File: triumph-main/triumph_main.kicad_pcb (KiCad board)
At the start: 2 copper layers, 99.1 x 86.4 mm, 83 parts, among them J1 JST_XH_vert_01x04, J10 JST_XH_vert_01x04, J2 JST_PH_vert_01x03, J3 JST_PH_vert_01x03, J4 JST_PH_vert_01x06, J5 Conn_BNC, J6 JST_PH_vert_01x03, J7 JST_PH_vert_01x06, J8 JST_PH_vert_01x03, J9 JST_PH_vert_01x03, Q1 J310, U1 LM211P, U2 NE5532AP, U3 NE5532AP, U4 NE5532AP, U5 NE5532AP

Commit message: Add onboard power LEDs
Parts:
- added D3: BLUE, triumph:LED_1206_HandSoldering, F.Cu at (133.1, 63.5)
- added D4: BLUE, triumph:LED_1206_HandSoldering, F.Cu at (156.0, 63.5)
- added R20: 10K, triumph:0805_R_HandSoldering, B.Cu at (133.1, 63.3)
- added R21: 10K, triumph:0805_R_HandSoldering, B.Cu at (156.0, 63.3)
- renumbered C12 to C10, C13 to C11, C14 to C12, C9 to C13, C10 to C14, C11 to C9, R20 to R22, R21 to R23, R22 to R24, R23 to R25
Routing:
- net +12V: track 269.0 -> 277.3 mm
- net -12V: track 247.1 -> 255.3 mm
- net Net-(D4-Pad2): track 0.00 -> 5.15 mm, vias 0 -> 1
- net Net-(D3-Pad1): track 0.00 -> 4.64 mm, vias 0 -> 1

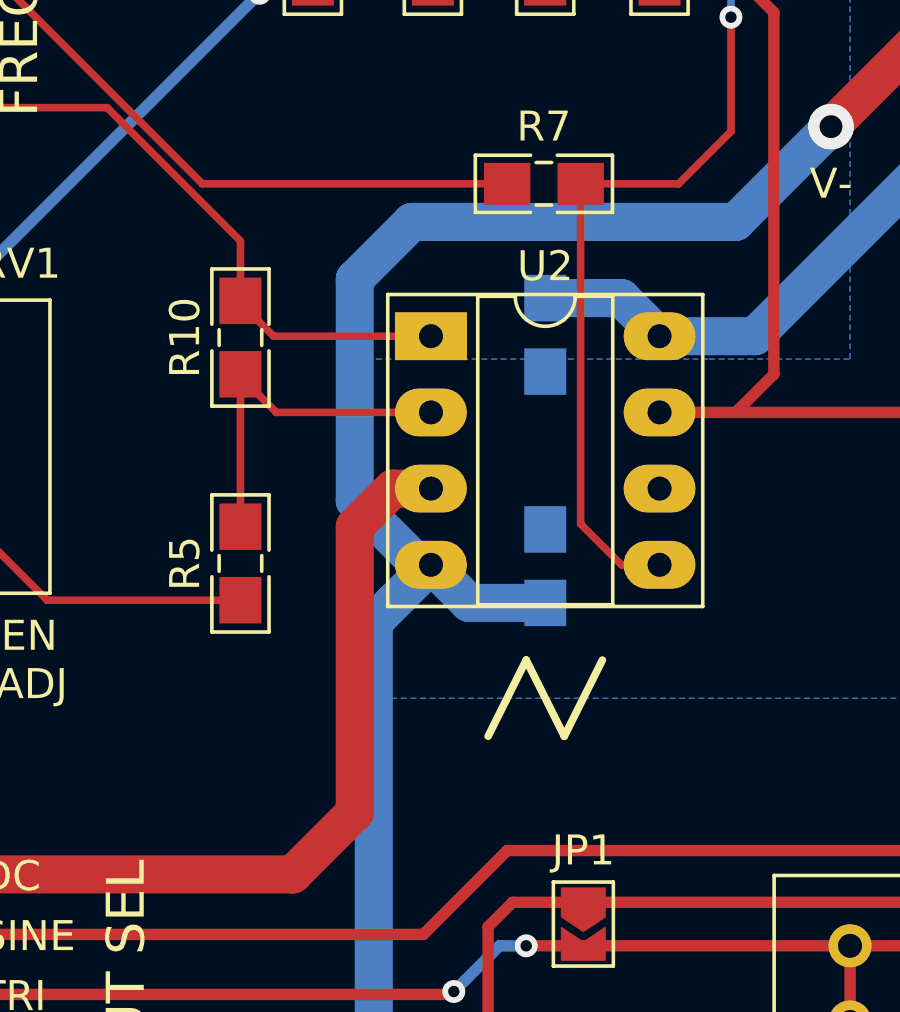
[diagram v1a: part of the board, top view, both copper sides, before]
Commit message: Correct triangle wave opamp orientation
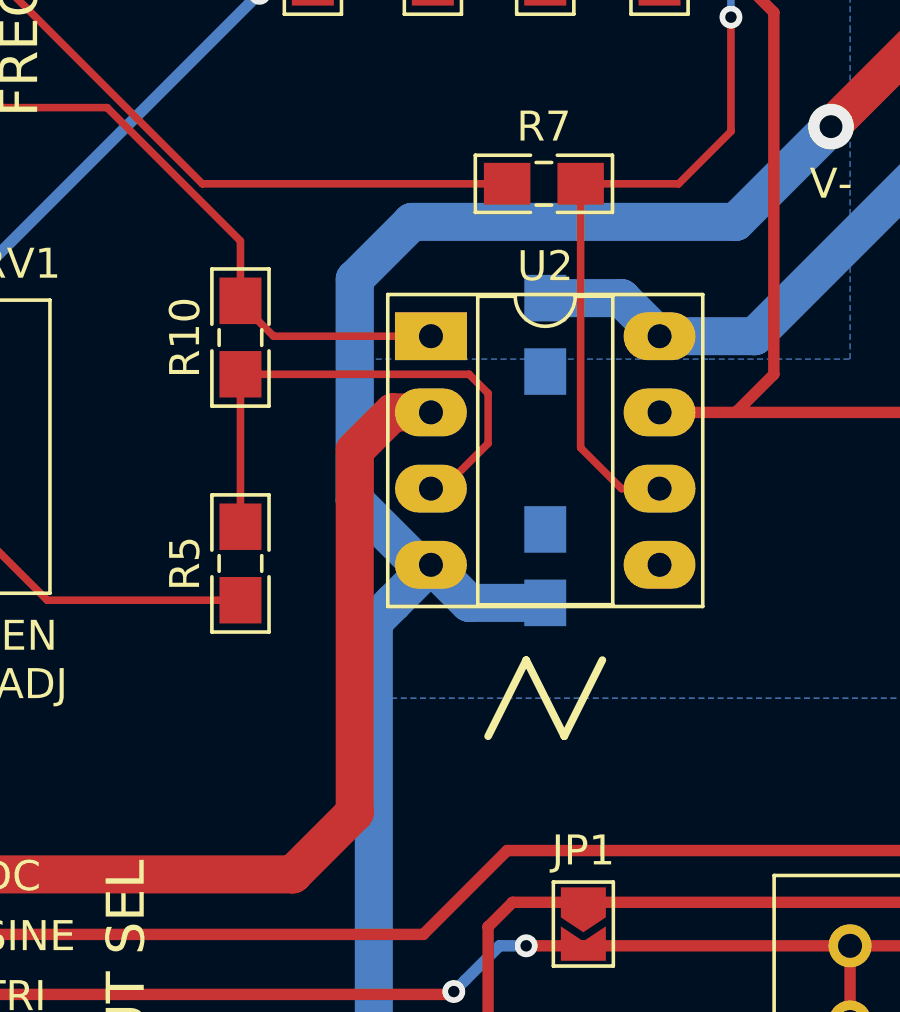
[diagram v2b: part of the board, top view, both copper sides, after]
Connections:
- U2 pad 2: Net-(R10-Pad1) -> GND
- U2 pad 3: GND -> Net-(R10-Pad1)
- U2 pad 5: /FC_COM -> GND
- U2 pad 6: GND -> /FC_COM
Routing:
- net Net-(R10-Pad1): track 12.0 -> 17.9 mm
- net GND: track 90.2 -> 92.7 mm
- net /FC_COM: track 47.9 -> 45.4 mm
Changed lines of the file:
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@@
     (thickness 1.6)
     (drawings 78)
-    (tracks 448)
+    (tracks 451)
     (zones 0)
     (modules 87)
@@
       (net 35 /SIG_TRI_RAW))
     (pad 3 thru_hole oval (at 0 5.08) (size 2.4 1.6) (drill 0.8) (layers *.Cu *.Mask)
-      (net 1 GND))
+      (net 26 "Net-(R10-Pad1)"))
     (pad 6 thru_hole oval (at 7.62 5.08) (size 2.4 1.6) (drill 0.8) (layers *.Cu *.Mask)
-      (net 1 GND))
+      (net 17 /FC_COM))
     (pad 2 thru_hole oval (at 0 2.54) (size 2.4 1.6) (drill 0.8) (layers *.Cu *.Mask)
-      (net 26 "Net-(R10-Pad1)"))
+      (net 1 GND))
     (pad 5 thru_hole oval (at 7.62 7.62) (size 2.4 1.6) (drill 0.8) (layers *.Cu *.Mask)
-      (net 17 /FC_COM))
+      (net 1 GND))
     (pad 1 thru_hole rect (at 0 0) (size 2.4 1.6) (drill 0.8) (layers *.Cu *.Mask)
       (net 7 /FR_1))
@@
   (segment (start 148.336 93.536) (end 151.066 93.536) (width 0.762) (layer F.Cu) (net 1))
   (segment (start 151.066 93.536) (end 153.416 93.536) (width 0.762) (layer F.Cu) (net 1))
-  (segment (start 116.586 88.646) (end 115.316 88.646) (width 1.27) (layer F.Cu) (net 1))
-  (segment (start 115.316 88.646) (end 114.046 89.916) (width 1.27) (layer F.Cu) (net 1))
-  (segment (start 114.046 89.916) (end 114.046 99.441) (width 1.27) (layer F.Cu) (net 1))
-  (segment (start 111.981 101.506) (end 98.171 101.506) (width 1.27) (layer F.Cu) (net 1))
-  (segment (start 114.046 99.441) (end 111.981 101.506) (width 1.27) (layer F.Cu) (net 1))
   (segment (start 169.936 134.356) (end 169.936 138.656) (width 1.27) (layer B.Cu) (net 1))
   (segment (start 170.901 125.771) (end 190.881 125.771) (width 1.27) (layer B.Cu) (net 1))
@@
   (segment (start 165.776 125.771) (end 163.871 125.771) (width 1.27) (layer B.Cu) (net 1))
   (via (at 138.811 76.581) (size 1.524) (drill 0.762) (layers F.Cu B.Cu) (net 1))
+  (segment (start 111.981 101.506) (end 98.171 101.506) (width 1.27) (layer F.Cu) (net 1))
+  (segment (start 114.046 99.441) (end 111.981 101.506) (width 1.27) (layer F.Cu) (net 1))
+  (segment (start 114.046 87.376) (end 114.046 99.441) (width 1.27) (layer F.Cu) (net 1))
+  (segment (start 116.586 86.106) (end 115.316 86.106) (width 1.27) (layer F.Cu) (net 1))
+  (segment (start 115.316 86.106) (end 114.046 87.376) (width 1.27) (layer F.Cu) (net 1))
   (segment (start 139.536 62.006) (end 140.836 60.706) (width 1.27) (layer B.Cu) (net 2))
   (segment (start 139.536 64.516) (end 139.536 62.006) (width 1.27) (layer B.Cu) (net 2))
@@
   (segment (start 116.586 62.611) (end 116.586 60.071) (width 0.254) (layer F.Cu) (net 16))
   (segment (start 112.651 66.546) (end 116.586 62.611) (width 0.254) (layer F.Cu) (net 16))
-  (segment (start 121.576 89.826) (end 121.576 78.486) (width 0.254) (layer F.Cu) (net 17))
-  (segment (start 124.206 91.186) (end 122.936 91.186) (width 0.254) (layer F.Cu) (net 17))
-  (segment (start 122.936 91.186) (end 121.576 89.826) (width 0.254) (layer F.Cu) (net 17))
   (segment (start 126.586 70.231) (end 126.586 60.071) (width 0.254) (layer F.Cu) (net 17))
   (segment (start 126.586 62.451) (end 126.586 70.231) (width 0.254) (layer F.Cu) (net 17))
@@
   (segment (start 126.586 70.769815) (end 126.586 72.931) (width 0.254) (layer B.Cu) (net 17))
   (segment (start 126.586 70.231) (end 126.586 70.769815) (width 0.254) (layer B.Cu) (net 17))
+  (segment (start 121.576 87.286) (end 121.576 78.486) (width 0.254) (layer F.Cu) (net 17))
+  (segment (start 124.206 88.646) (end 122.936 88.646) (width 0.254) (layer F.Cu) (net 17))
+  (segment (start 122.936 88.646) (end 121.576 87.286) (width 0.254) (layer F.Cu) (net 17))
   (segment (start 122.936 116.586) (end 124.296 116.586) (width 0.254) (layer F.Cu) (net 18))
   (segment (start 121.666 121.666) (end 121.666 117.856) (width 0.254) (layer F.Cu) (net 18))
@@
   (segment (start 145.796 84.646) (end 145.796 80.836) (width 0.254) (layer F.Cu) (net 25))
   (segment (start 110.236 84.911) (end 110.236 84.836) (width 0.254) (layer F.Cu) (net 26))
-  (segment (start 111.431 86.106) (end 110.236 84.911) (width 0.254) (layer F.Cu) (net 26))
-  (segment (start 116.586 86.106) (end 111.431 86.106) (width 0.254) (layer F.Cu) (net 26))
   (segment (start 110.236 88.887) (end 110.236 84.836) (width 0.254) (layer F.Cu) (net 26))
   (segment (start 110.236 89.916) (end 110.236 88.887) (width 0.254) (layer F.Cu) (net 26))
+  (segment (start 110.236 84.836) (end 117.856 84.836) (width 0.254) (layer F.Cu) (net 26))
+  (segment (start 117.856 84.836) (end 118.491 85.471) (width 0.254) (layer F.Cu) (net 26))
+  (segment (start 118.491 85.471) (end 118.491 87.141) (width 0.254) (layer F.Cu) (net 26))
+  (segment (start 116.986 88.646) (end 116.586 88.646) (width 0.254) (layer F.Cu) (net 26))
+  (segment (start 118.491 87.141) (end 116.986 88.646) (width 0.254) (layer F.Cu) (net 26))
   (segment (start 101.346 89.916) (end 101.346 89.789) (width 0.254) (layer F.Cu) (net 27))
   (segment (start 110.236 92.366) (end 103.796 92.366) (width 0.254) (layer F.Cu) (net 27))
